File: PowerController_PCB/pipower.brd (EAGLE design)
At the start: 70.8 x 17.7 mm, 25 parts, among them IC1 12F629, Q1 AP4435GH, Q2 AP4435GH, T1 BC848, T2 BC848, T3 BC848, X1 22-23-2021, X2 22-23-2021

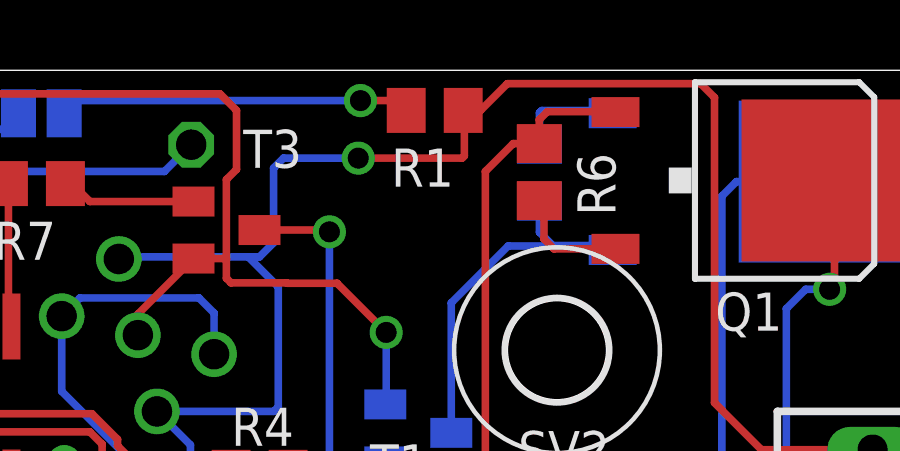
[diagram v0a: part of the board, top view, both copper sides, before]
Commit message: Added files via upload
faltaba una pista
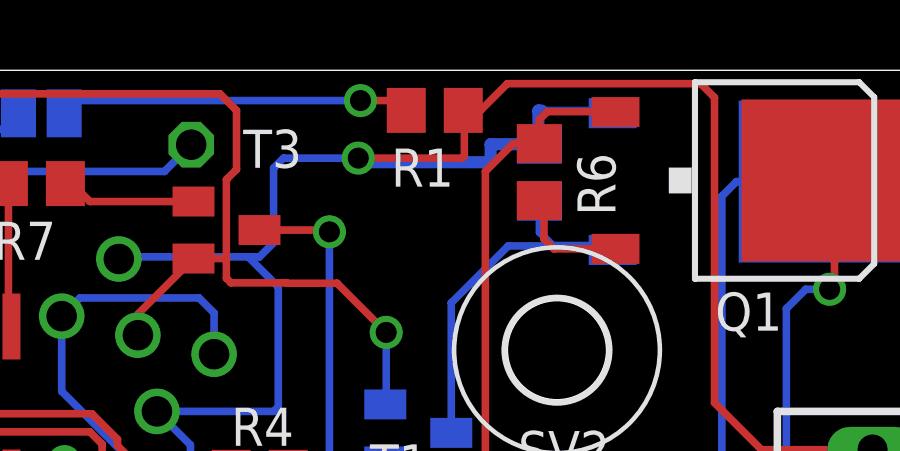
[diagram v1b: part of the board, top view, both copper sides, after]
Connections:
- removed net N$12: Q1.3, R6.2
- removed net N$4: Q2.3, R5.2
- net VDD: now also Q1.3, Q2.3, R5.2, R6.2
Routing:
- net VDD: track 123.5 -> 138.9 mm
- net N$12: track 3.86 -> 0.00 mm
- net N$4: track 3.56 -> 0.00 mm
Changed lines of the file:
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@@
 <grid distance="0.003125" unitdist="mic" unit="mm" style="lines" multiple="1" display="no" altdistance="0.003125" altunitdist="mic" altunit="mm"/>
 <layers>
-<layer number="1" name="Top" color="4" fill="1" visible="no" active="yes"/>
+<layer number="1" name="Top" color="4" fill="1" visible="yes" active="yes"/>
 <layer number="2" name="Route2" color="1" fill="3" visible="no" active="no"/>
 <layer number="3" name="Route3" color="4" fill="3" visible="no" active="no"/>
@@
 <layer number="14" name="Route14" color="1" fill="6" visible="no" active="no"/>
 <layer number="15" name="Route15" color="4" fill="6" visible="no" active="no"/>
-<layer number="16" name="Bottom" color="1" fill="1" visible="no" active="yes"/>
+<layer number="16" name="Bottom" color="1" fill="1" visible="yes" active="yes"/>
 <layer number="17" name="Pads" color="2" fill="1" visible="yes" active="yes"/>
-<layer number="18" name="Vias" color="2" fill="1" visible="no" active="yes"/>
+<layer number="18" name="Vias" color="2" fill="1" visible="yes" active="yes"/>
 <layer number="19" name="Unrouted" color="6" fill="1" visible="yes" active="yes"/>
 <layer number="20" name="Dimension" color="15" fill="1" visible="yes" active="yes"/>
@@
 <wire x1="24.84285" y1="14.460178125" x2="25.174975" y2="14.792303125" width="0.254" layer="16"/>
 <wire x1="25.174975" y1="14.792303125" x2="27.666203125" y2="14.792303125" width="0.254" layer="16"/>
+<contactref element="Q1" pad="3"/>
+<contactref element="R6" pad="2"/>
+<wire x1="33.700209375" y1="13.376625" x2="33.85518125" y2="13.221653125" width="0.254" layer="1"/>
+<wire x1="33.85518125" y1="13.221653125" x2="33.85518125" y2="12.099440625" width="0.254" layer="1"/>
+<wire x1="33.85518125" y1="12.099440625" x2="34.187575" y2="11.767046875" width="0.254" layer="1"/>
+<wire x1="34.187575" y1="11.767046875" x2="36.23956875" y2="11.767046875" width="0.254" layer="1"/>
+<contactref element="Q2" pad="3"/>
+<contactref element="R5" pad="2"/>
+<wire x1="36.146190625" y1="16.289803125" x2="36.057484375" y2="16.378509375" width="0.254" layer="16"/>
+<wire x1="36.057484375" y1="16.378509375" x2="33.781503125" y2="16.378509375" width="0.254" layer="16"/>
+<wire x1="33.781503125" y1="16.378509375" x2="33.706196875" y2="16.303203125" width="0.254" layer="16"/>
+<wire x1="33.706196875" y1="16.303203125" x2="33.706196875" y2="15.254034375" width="0.254" layer="16"/>
+<wire x1="33.781503125" y1="16.378509375" x2="33.67025" y2="16.378509375" width="0.4064" layer="16"/>
+<wire x1="33.67025" y1="16.378509375" x2="33.67025" y2="15.255309375" width="0.4064" layer="16"/>
+<wire x1="33.67025" y1="15.255309375" x2="32.077278125" y2="15.255309375" width="0.4064" layer="16"/>
+<wire x1="32.077278125" y1="15.255309375" x2="32.077278125" y2="14.655459375" width="0.4064" layer="16"/>
+<wire x1="32.077278125" y1="14.655459375" x2="27.666203125" y2="14.655459375" width="0.4064" layer="16"/>
+<wire x1="27.666203125" y1="14.655459375" x2="27.666203125" y2="14.792303125" width="0.4064" layer="16"/>
+<wire x1="33.706196875" y1="15.254034375" x2="33.700209375" y2="13.376625" width="0" layer="19" extent="1-16"/>
 </signal>
 <signal name="N$10">
@@
 <wire x1="30.766240625" y1="9.966346875" x2="30.766240625" y2="5.63325" width="0.254" layer="16"/>
 </signal>
-<signal name="N$4">
-<contactref element="Q2" pad="3"/>
-<contactref element="R5" pad="2"/>
-<wire x1="36.146190625" y1="16.289803125" x2="36.057484375" y2="16.378509375" width="0.254" layer="16"/>
-<wire x1="36.057484375" y1="16.378509375" x2="33.781503125" y2="16.378509375" width="0.254" layer="16"/>
-<wire x1="33.781503125" y1="16.378509375" x2="33.706196875" y2="16.303203125" width="0.254" layer="16"/>
-<wire x1="33.706196875" y1="16.303203125" x2="33.706196875" y2="15.254034375" width="0.254" layer="16"/>
-</signal>
 <signal name="N$8">
 <contactref element="Q2" pad="4"/>
@@
 <wire x1="40.272178125" y1="14.009803125" x2="43.446190625" y2="14.009803125" width="0.254" layer="16"/>
 </signal>
-<signal name="N$12">
-<contactref element="Q1" pad="3"/>
-<contactref element="R6" pad="2"/>
-<wire x1="33.700209375" y1="13.376625" x2="33.85518125" y2="13.221653125" width="0.254" layer="1"/>
-<wire x1="33.85518125" y1="13.221653125" x2="33.85518125" y2="12.099440625" width="0.254" layer="1"/>
-<wire x1="33.85518125" y1="12.099440625" x2="34.187575" y2="11.767046875" width="0.254" layer="1"/>
-<wire x1="34.187575" y1="11.767046875" x2="36.23956875" y2="11.767046875" width="0.254" layer="1"/>
-</signal>
 <signal name="N$9">
